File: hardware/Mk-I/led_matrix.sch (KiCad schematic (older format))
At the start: 34 parts, among them U9 SSD1306

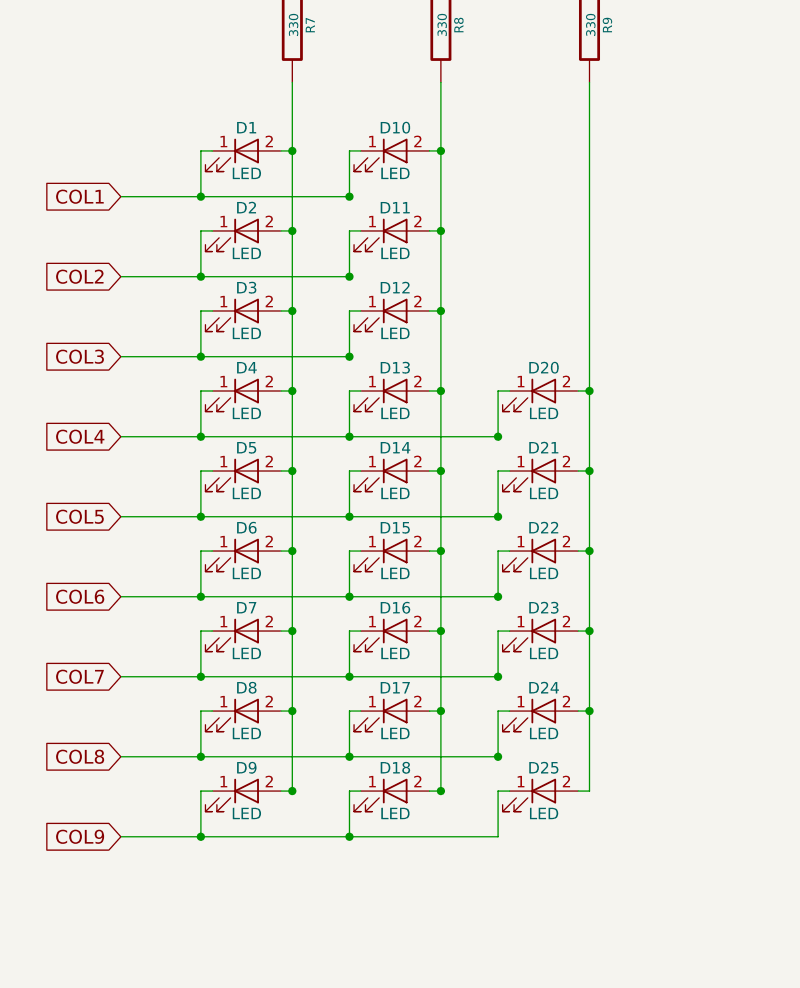
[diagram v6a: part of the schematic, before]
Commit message: HW: Update parts value
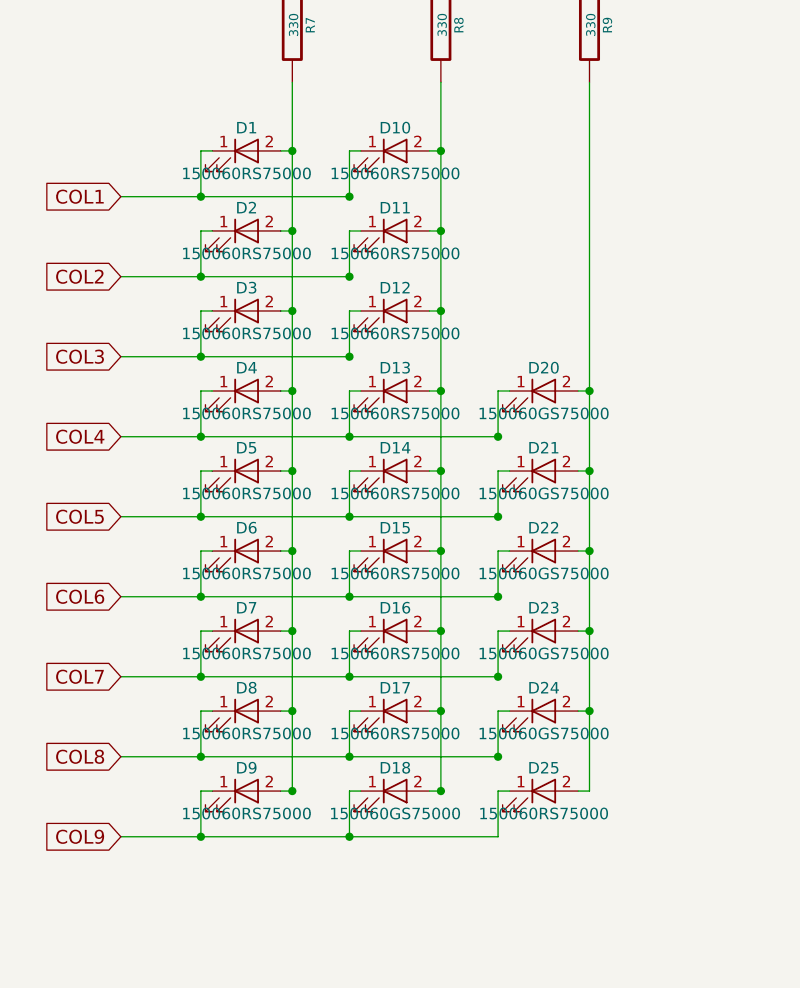
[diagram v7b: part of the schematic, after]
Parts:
- D1, D10, D11, D12, D13, D14, D15, D16, D17, D2, D25, D3, D4, D5, D6, D7, D8, D9: value LED -> 150060RS75000
- D18, D20, D21, D22, D23, D24: value LED -> 150060GS75000
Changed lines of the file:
@@
 AR Path="/585D6FEE/585D8A6E" Ref="D10"  Part="1"
 F 0 "D10" H 2650 2550 50  0000 C CNN
-F 1 "LED" H 2650 2350 50  0000 C CNN
+F 1 "150060RS75000" H 2650 2350 50  0000 C CNN
 F 2 "LEDs:LED_0805" H 2650 2450 50  0001 C CNN
 F 3 "" H 2650 2450 50  0000 C CNN
@@
 AR Path="/585D6FEE/585D8A75" Ref="D11"  Part="1"
 F 0 "D11" H 2650 2900 50  0000 C CNN
-F 1 "LED" H 2650 2700 50  0000 C CNN
+F 1 "150060RS75000" H 2650 2700 50  0000 C CNN
 F 2 "LEDs:LED_0805" H 2650 2800 50  0001 C CNN
 F 3 "" H 2650 2800 50  0000 C CNN
@@
 AR Path="/585D6FEE/585D8A7C" Ref="D12"  Part="1"
 F 0 "D12" H 2650 3250 50  0000 C CNN
-F 1 "LED" H 2650 3050 50  0000 C CNN
+F 1 "150060RS75000" H 2650 3050 50  0000 C CNN
 F 2 "LEDs:LED_0805" H 2650 3150 50  0001 C CNN
 F 3 "" H 2650 3150 50  0000 C CNN
@@
 AR Path="/585D6FEE/585D8A83" Ref="D13"  Part="1"
 F 0 "D13" H 2650 3600 50  0000 C CNN
-F 1 "LED" H 2650 3400 50  0000 C CNN
+F 1 "150060RS75000" H 2650 3400 50  0000 C CNN
 F 2 "LEDs:LED_0805" H 2650 3500 50  0001 C CNN
 F 3 "" H 2650 3500 50  0000 C CNN
@@
 AR Path="/585D6FEE/585D8A8A" Ref="D14"  Part="1"
 F 0 "D14" H 2650 3950 50  0000 C CNN
-F 1 "LED" H 2650 3750 50  0000 C CNN
+F 1 "150060RS75000" H 2650 3750 50  0000 C CNN
 F 2 "LEDs:LED_0805" H 2650 3850 50  0001 C CNN
 F 3 "" H 2650 3850 50  0000 C CNN
@@
 AR Path="/585D6FEE/585D8A91" Ref="D1"  Part="1"
 F 0 "D1" H 2000 2550 50  0000 C CNN
-F 1 "LED" H 2000 2350 50  0000 C CNN
+F 1 "150060RS75000" H 2000 2350 50  0000 C CNN
 F 2 "LEDs:LED_0805" H 2000 2450 50  0001 C CNN
 F 3 "" H 2000 2450 50  0000 C CNN
@@
 AR Path="/585D6FEE/585D8A98" Ref="D2"  Part="1"
 F 0 "D2" H 2000 2900 50  0000 C CNN
-F 1 "LED" H 2000 2700 50  0000 C CNN
+F 1 "150060RS75000" H 2000 2700 50  0000 C CNN
 F 2 "LEDs:LED_0805" H 2000 2800 50  0001 C CNN
 F 3 "" H 2000 2800 50  0000 C CNN
@@
 AR Path="/585D6FEE/585D8A9F" Ref="D3"  Part="1"
 F 0 "D3" H 2000 3250 50  0000 C CNN
-F 1 "LED" H 2000 3050 50  0000 C CNN
+F 1 "150060RS75000" H 2000 3050 50  0000 C CNN
 F 2 "LEDs:LED_0805" H 2000 3150 50  0001 C CNN
 F 3 "" H 2000 3150 50  0000 C CNN
@@
 AR Path="/585D6FEE/585D8AA6" Ref="D4"  Part="1"
 F 0 "D4" H 2000 3600 50  0000 C CNN
-F 1 "LED" H 2000 3400 50  0000 C CNN
+F 1 "150060RS75000" H 2000 3400 50  0000 C CNN
 F 2 "LEDs:LED_0805" H 2000 3500 50  0001 C CNN
 F 3 "" H 2000 3500 50  0000 C CNN
@@
 AR Path="/585D6FEE/585D8AAD" Ref="D5"  Part="1"
 F 0 "D5" H 2000 3950 50  0000 C CNN
-F 1 "LED" H 2000 3750 50  0000 C CNN
+F 1 "150060RS75000" H 2000 3750 50  0000 C CNN
 F 2 "LEDs:LED_0805" H 2000 3850 50  0001 C CNN
 F 3 "" H 2000 3850 50  0000 C CNN
@@
 AR Path="/585D6FEE/585D8AB4" Ref="D6"  Part="1"
 F 0 "D6" H 2000 4300 50  0000 C CNN
-F 1 "LED" H 2000 4100 50  0000 C CNN
+F 1 "150060RS75000" H 2000 4100 50  0000 C CNN
 F 2 "LEDs:LED_0805" H 2000 4200 50  0001 C CNN
 F 3 "" H 2000 4200 50  0000 C CNN
@@
 AR Path="/585D6FEE/585D8ABB" Ref="D7"  Part="1"
 F 0 "D7" H 2000 4650 50  0000 C CNN
-F 1 "LED" H 2000 4450 50  0000 C CNN
+F 1 "150060RS75000" H 2000 4450 50  0000 C CNN
 F 2 "LEDs:LED_0805" H 2000 4550 50  0001 C CNN
 F 3 "" H 2000 4550 50  0000 C CNN
@@
 AR Path="/585D6FEE/585D8AC2" Ref="D8"  Part="1"
 F 0 "D8" H 2000 5000 50  0000 C CNN
-F 1 "LED" H 2000 4800 50  0000 C CNN
+F 1 "150060RS75000" H 2000 4800 50  0000 C CNN
 F 2 "LEDs:LED_0805" H 2000 4900 50  0001 C CNN
 F 3 "" H 2000 4900 50  0000 C CNN
@@
 AR Path="/585D6FEE/585D8AC9" Ref="D9"  Part="1"
 F 0 "D9" H 2000 5350 50  0000 C CNN
-F 1 "LED" H 2000 5150 50  0000 C CNN
+F 1 "150060RS75000" H 2000 5150 50  0000 C CNN
 F 2 "LEDs:LED_0805" H 2000 5250 50  0001 C CNN
 F 3 "" H 2000 5250 50  0000 C CNN
@@
 AR Path="/585D6FEE/585D8AD0" Ref="D25"  Part="1"
 F 0 "D25" H 3300 5350 50  0000 C CNN
-F 1 "LED" H 3300 5150 50  0000 C CNN
+F 1 "150060RS75000" H 3300 5150 50  0000 C CNN
 F 2 "LEDs:LED_0805" H 3300 5250 50  0001 C CNN
 F 3 "" H 3300 5250 50  0000 C CNN
@@
 AR Path="/585D6FEE/585D8ADE" Ref="D20"  Part="1"
 F 0 "D20" H 3300 3600 50  0000 C CNN
-F 1 "LED" H 3300 3400 50  0000 C CNN
+F 1 "150060GS75000" H 3300 3400 50  0000 C CNN
 F 2 "LEDs:LED_0805" H 3300 3500 50  0001 C CNN
 F 3 "" H 3300 3500 50  0000 C CNN
@@
 AR Path="/585D6FEE/585D8AE5" Ref="D21"  Part="1"
 F 0 "D21" H 3300 3950 50  0000 C CNN
-F 1 "LED" H 3300 3750 50  0000 C CNN
+F 1 "150060GS75000" H 3300 3750 50  0000 C CNN
 F 2 "LEDs:LED_0805" H 3300 3850 50  0001 C CNN
 F 3 "" H 3300 3850 50  0000 C CNN
@@
 AR Path="/585D6FEE/585D8AEC" Ref="D22"  Part="1"
 F 0 "D22" H 3300 4300 50  0000 C CNN
-F 1 "LED" H 3300 4100 50  0000 C CNN
+F 1 "150060GS75000" H 3300 4100 50  0000 C CNN
 F 2 "LEDs:LED_0805" H 3300 4200 50  0001 C CNN
 F 3 "" H 3300 4200 50  0000 C CNN
@@
 AR Path="/585D6FEE/585D8AF3" Ref="D23"  Part="1"
 F 0 "D23" H 3300 4650 50  0000 C CNN
-F 1 "LED" H 3300 4450 50  0000 C CNN
+F 1 "150060GS75000" H 3300 4450 50  0000 C CNN
 F 2 "LEDs:LED_0805" H 3300 4550 50  0001 C CNN
 F 3 "" H 3300 4550 50  0000 C CNN
@@
 AR Path="/585D6FEE/585D8AFA" Ref="D15"  Part="1"
 F 0 "D15" H 2650 4300 50  0000 C CNN
-F 1 "LED" H 2650 4100 50  0000 C CNN
+F 1 "150060RS75000" H 2650 4100 50  0000 C CNN
 F 2 "LEDs:LED_0805" H 2650 4200 50  0001 C CNN
 F 3 "" H 2650 4200 50  0000 C CNN
@@
 AR Path="/585D6FEE/585D8B01" Ref="D16"  Part="1"
 F 0 "D16" H 2650 4650 50  0000 C CNN
-F 1 "LED" H 2650 4450 50  0000 C CNN
+F 1 "150060RS75000" H 2650 4450 50  0000 C CNN
 F 2 "LEDs:LED_0805" H 2650 4550 50  0001 C CNN
 F 3 "" H 2650 4550 50  0000 C CNN
@@
 AR Path="/585D6FEE/585D8B08" Ref="D17"  Part="1"
 F 0 "D17" H 2650 5000 50  0000 C CNN
-F 1 "LED" H 2650 4800 50  0000 C CNN
+F 1 "150060RS75000" H 2650 4800 50  0000 C CNN
 F 2 "LEDs:LED_0805" H 2650 4900 50  0001 C CNN
 F 3 "" H 2650 4900 50  0000 C CNN
@@
 AR Path="/585D6FEE/585D8B0F" Ref="D18"  Part="1"
 F 0 "D18" H 2650 5350 50  0000 C CNN
-F 1 "LED" H 2650 5150 50  0000 C CNN
+F 1 "150060GS75000" H 2650 5150 50  0000 C CNN
 F 2 "LEDs:LED_0805" H 2650 5250 50  0001 C CNN
 F 3 "" H 2650 5250 50  0000 C CNN
@@
 AR Path="/585D6FEE/585D8B16" Ref="D24"  Part="1"
 F 0 "D24" H 3300 5000 50  0000 C CNN
-F 1 "LED" H 3300 4800 50  0000 C CNN
+F 1 "150060GS75000" H 3300 4800 50  0000 C CNN
 F 2 "LEDs:LED_0805" H 3300 4900 50  0001 C CNN
 F 3 "" H 3300 4900 50  0000 C CNN
